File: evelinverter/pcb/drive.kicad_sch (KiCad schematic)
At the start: 35 parts, among them Q1 AON7418, Q2 AON7418, Q3 AON7418, Q4 AON7418, Q5 AON7418, Q6 AON7418, U2 DRV8300DRGE, U3 INA186, U4 INA186, U5 INA186

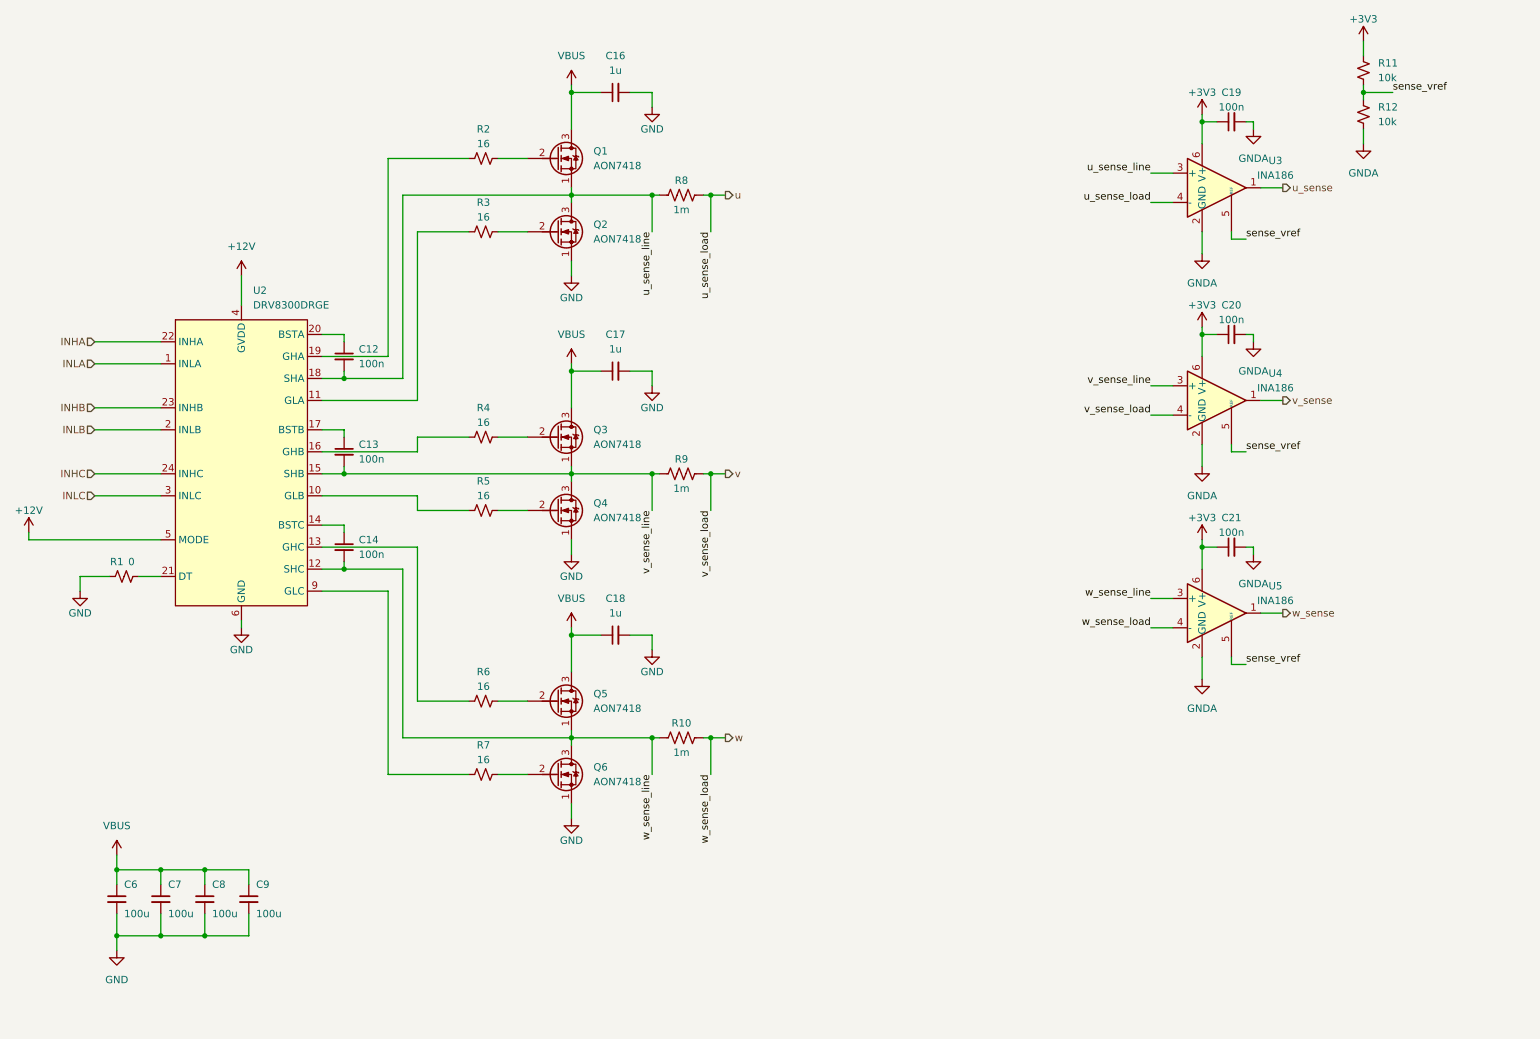
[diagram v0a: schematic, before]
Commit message: started redoing evelinverter
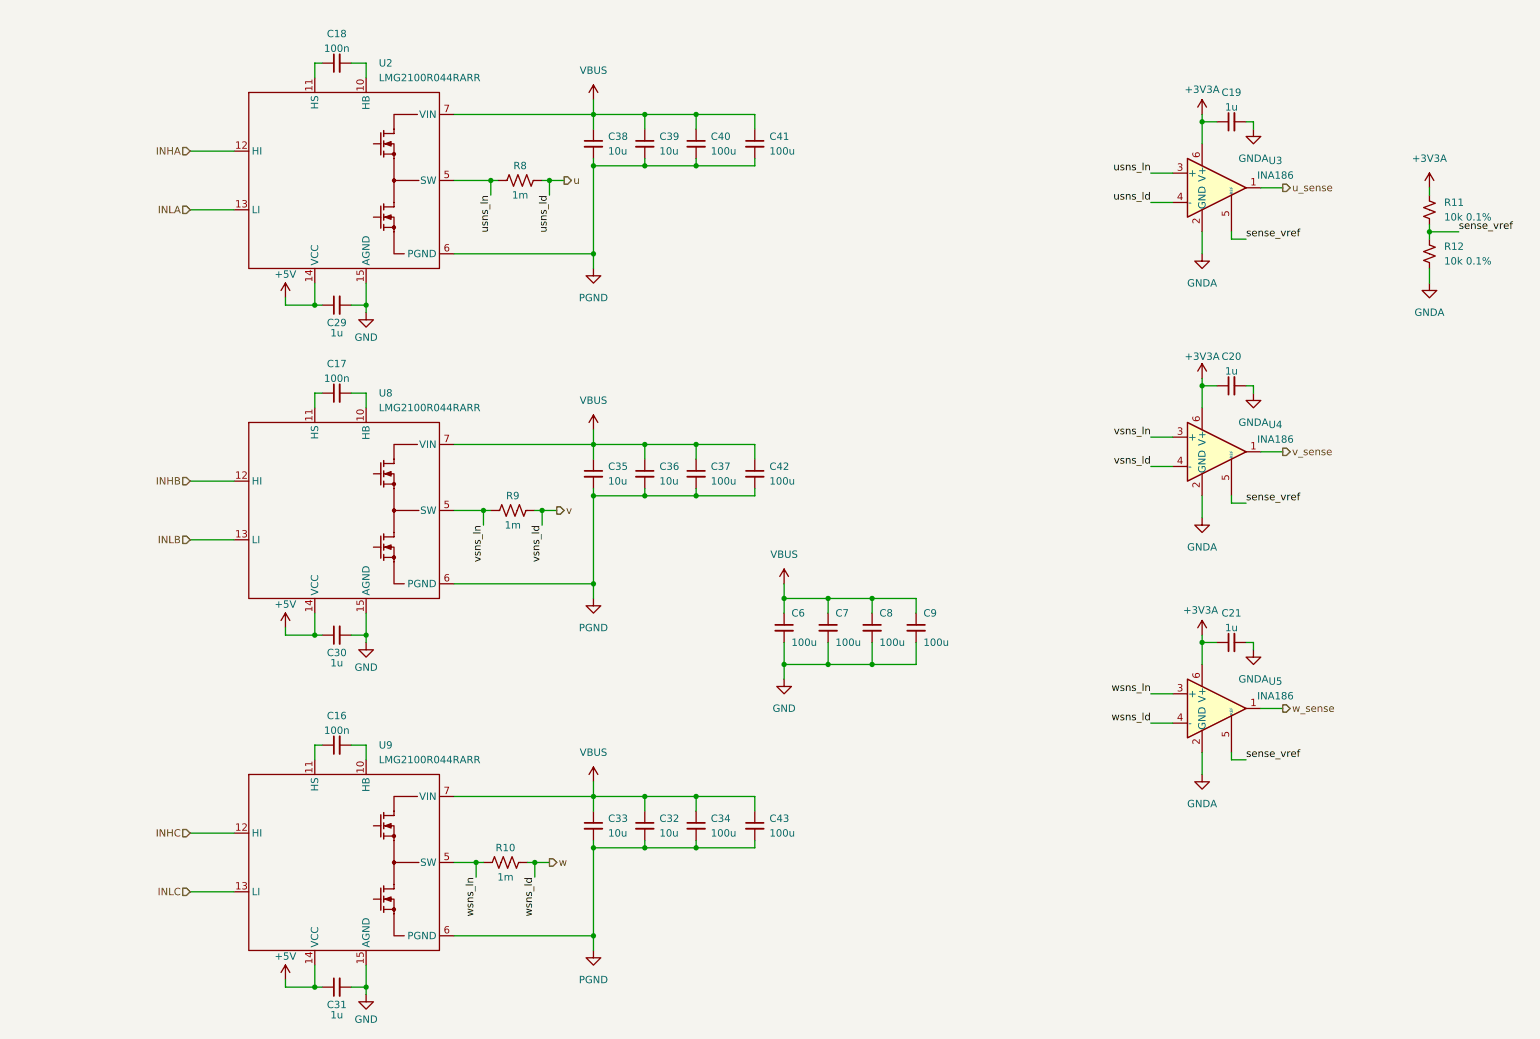
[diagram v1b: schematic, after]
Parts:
- removed C12, C13, C14: 100n, Capacitor_SMD:C_0603_1608Metric, symbol Device:C_Small
- removed Q1, Q2, Q3, Q4, Q5, Q6: AON7418, a22verter:DFN3.3x3.3-EP, symbol Device:Q_NMOS_SGD
- removed R1: 0, Resistor_SMD:R_0402_1005Metric, symbol Device:R_Small_US
- removed R2, R3, R4, R5, R6, R7: 16, Resistor_SMD:R_0402_1005Metric, symbol Device:R_Small_US
- removed U2: DRV8300DRGE, Package_DFN_QFN:VQFN-24-1EP_4x4mm_P0.5mm_EP2.45x2.45mm, symbol a22verter:DRV8300
- added C29, C30, C31: 1u, symbol Device:C_Small
- added C32, C33, C35, C36, C38, C39: 10u, symbol Device:C_Small
- added C34, C37, C40, C41, C42, C43: 100u, symbol Device:C_Small
- added U2, U8, U9: LMG2100R044RARR, evelyn:ICS-000009-EV, symbol #inventree:LMG2100R044
- C16, C17, C18: value 1u -> 100n; footprint Capacitor_SMD:C_1206_3216Metric -> Capacitor_SMD:C_0402_1005Metric
- C19, C20, C21: value 100n -> 1u
- R11, R12: value 10k -> 10k 0.1%
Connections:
- net GND: now also C29.2, C30.2, C31.2, U2.15 (AGND), U8.15 (AGND), U9.15 (AGND); no longer C16.2, C17.2, C18.2
- net INHA: now also U2.12 (HI)
- net INHB: now also U8.12 (HI)
- net INHC: now also U9.12 (HI)
- net INLA: now also U2.13 (LI)
- net INLB: now also U8.13 (LI)
- net INLC: now also U9.13 (LI)
- net VBUS: now also C32.1, C33.1, C34.1, C35.1, C36.1, C37.1, C38.1, C39.1, C40.1, C41.1, C42.1, C43.1, U2.7 (VIN), U8.7 (VIN), U9.7 (VIN); no longer C16.1, C17.1, C18.1
- net +3V3 renamed +3V3A
- net u_sense_line renamed usns_ln
- net usns_ln: now also U2.5 (SW)
- net v_sense_line renamed vsns_ln
- net vsns_ln: now also U8.5 (SW)
- net w_sense_line renamed wsns_ln
- net wsns_ln: now also U9.5 (SW)
- new net: U9.1 (NC), U9.16 (NC), U9.2 (NC), U9.3 (NC), U9.4 (NC), U9.8 (NC), U9.9 (NC)
- new net: C16.2, U9.10 (HB)
- new net: C16.1, U9.11 (HS)
- new net: C18.1, U2.11 (HS)
- new net: C18.2, U2.10 (HB)
- new net: U8.1 (NC), U8.16 (NC), U8.2 (NC), U8.3 (NC), U8.4 (NC), U8.8 (NC), U8.9 (NC)
- new net: C17.2, U8.10 (HB)
- new net: C17.1, U8.11 (HS)
- new net: U2.1 (NC), U2.16 (NC), U2.2 (NC), U2.3 (NC), U2.4 (NC), U2.8 (NC), U2.9 (NC)
- new net +5V: C29.1, C30.1, C31.1, U2.14 (VCC), U8.14 (VCC), U9.14 (VCC)
- new net PGND: C32.2, C33.2, C34.2, C35.2, C36.2, C37.2, C38.2, C39.2, C40.2, C41.2, C42.2, C43.2, U2.17 (PGND), U2.6 (PGND), U8.17 (PGND), U8.6 (PGND), U9.17 (PGND), U9.6 (PGND)
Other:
- moved on the sheet: C20, C21, C6, C7, C8, C9, R10, R11, R12, R8, R9, U4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
